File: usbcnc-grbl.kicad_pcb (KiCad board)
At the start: 2 copper layers, 55.2 x 48 mm, 10 parts, among them J1 USB_B, J2 DB9_Female, J3 DB25_Female, U1 YAAJ_BluePill

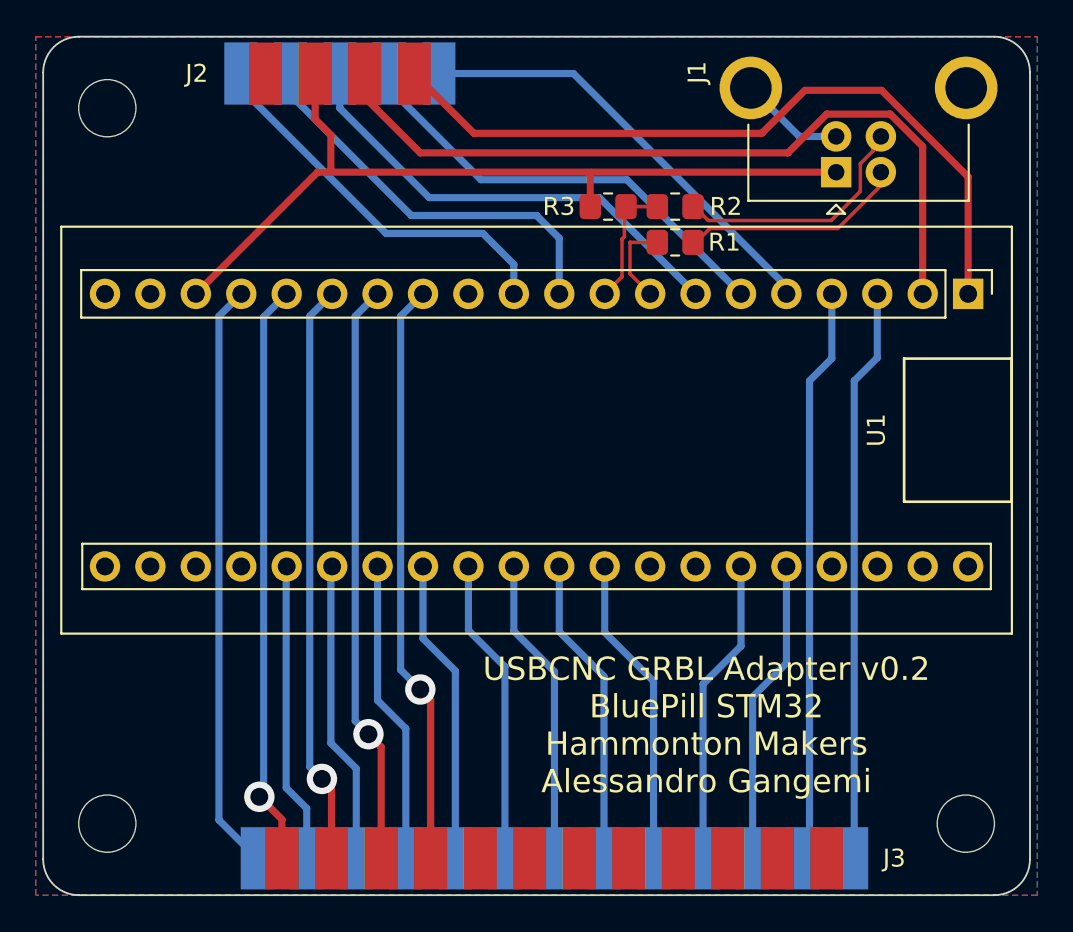
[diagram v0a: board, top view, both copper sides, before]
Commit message: Fix pullup on USB
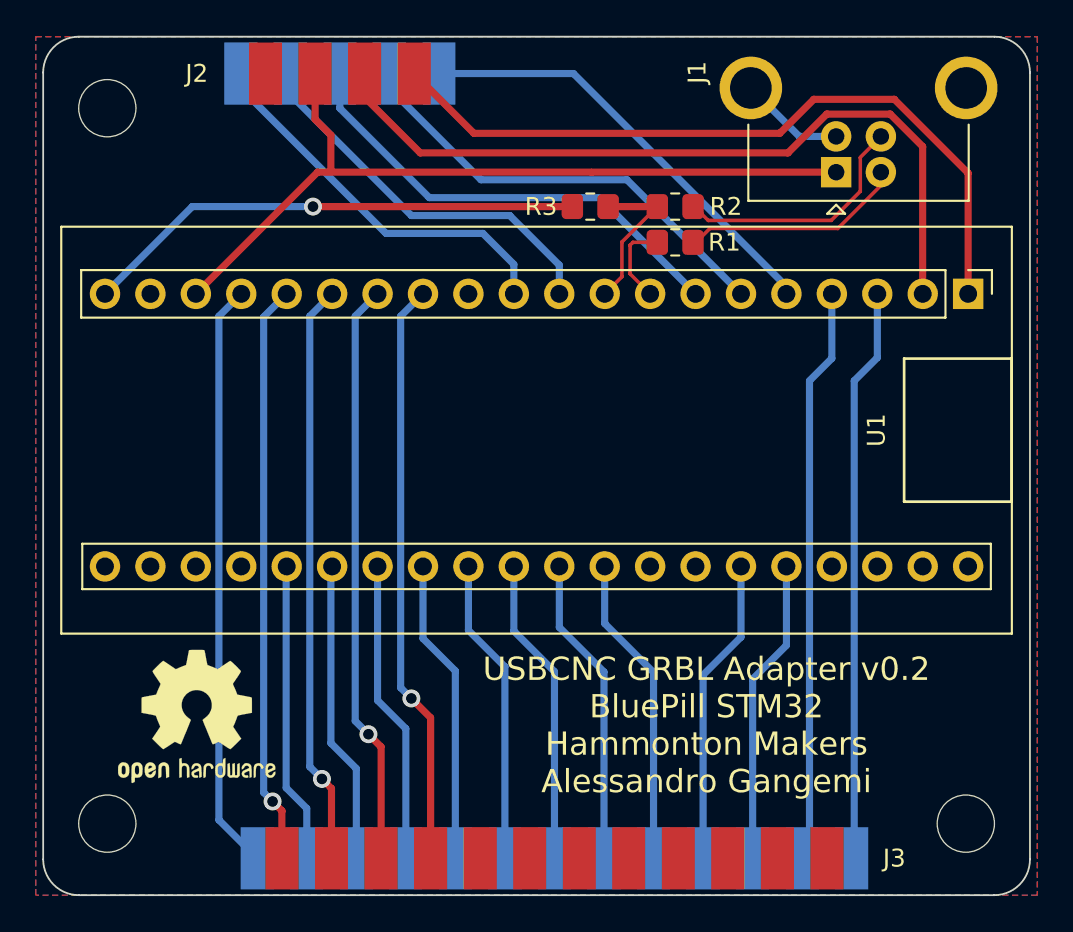
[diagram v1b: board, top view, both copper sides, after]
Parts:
- added REF**: OSHW-Logo2_9.8x8mm_SilkScreen, Symbol:OSHW-Logo2_9.8x8mm_SilkScreen, F.Cu at (80.0, 77.0)
- R3: value 4.7k -> 1.5k
- moved R3 1.00 mm to (102.0, 48.5)
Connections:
- R3 pad 1: +5V -> +3V3
- U1 pad 20: unconnected-(U1-Pad20) -> +3V3
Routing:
- net +3V3: track 0.00 -> 28.2 mm, vias 0 -> 1
- net +5V: track 46.3 -> 44.4 mm
- net USB+: track 7.42 -> 8.85 mm
- net PA15: track 22.6 -> 21.8 mm
